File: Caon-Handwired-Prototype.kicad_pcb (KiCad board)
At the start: 6 copper layers, 28 parts, among them SW4 EC11 ENCODER 1, SW8 EC11 ENCODER 1, U1 74HC595, U2 74HC595, U3 SuperMini nRF52840

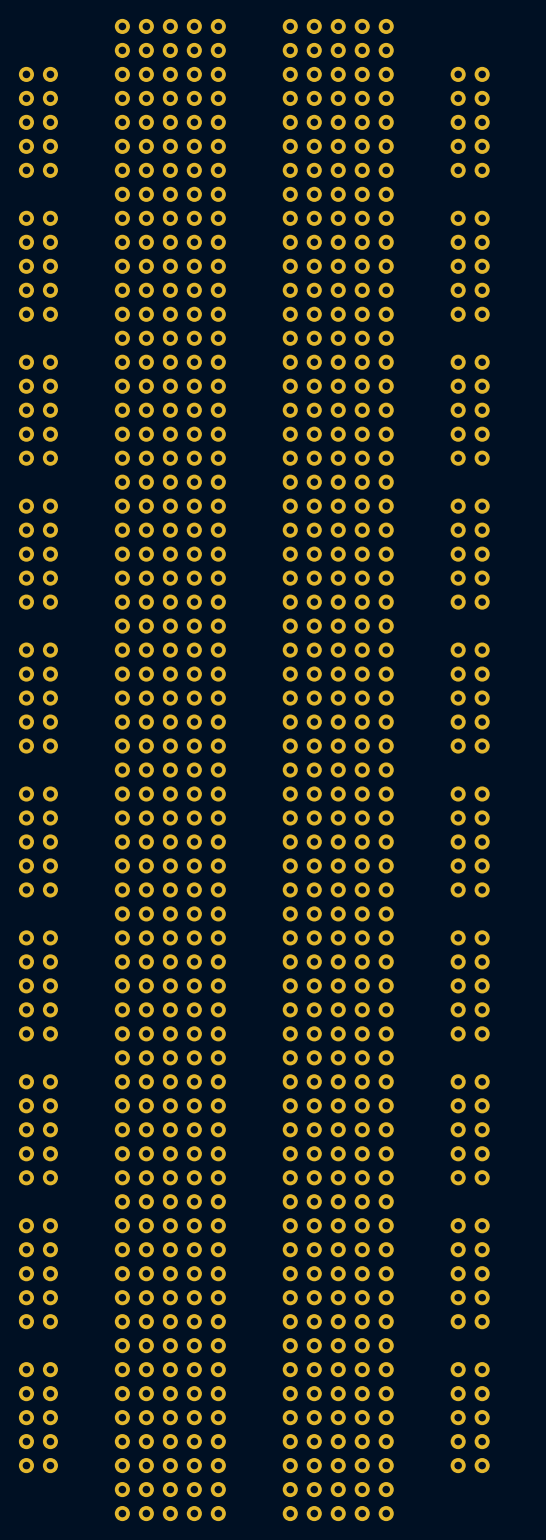
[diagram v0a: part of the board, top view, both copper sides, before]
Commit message: fix: 2nd 595 as 2nd Device
instead of daisy chained
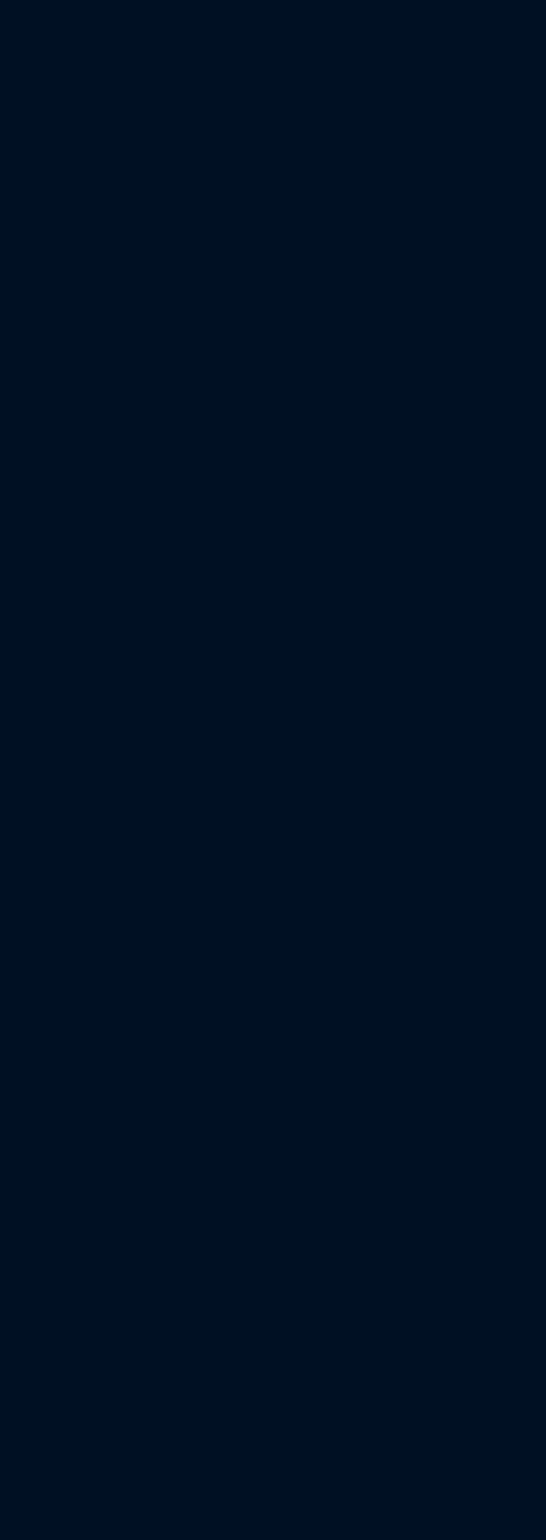
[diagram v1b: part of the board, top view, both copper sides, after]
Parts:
- removed REF**: Standard 830 Breadboard, Caon_Footprint:Standard 830 Breadboard
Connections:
- U1 pad 9: unconnected-(U1-QH&apos;-Pad9) -> QH'
- U2 pad 14: MOSI -> QH'
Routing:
- net MOSI: track 78.7 -> 48.3 mm
- net QH': track 0.00 -> 25.4 mm

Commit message: Schematic and PCB Update
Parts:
- added J1: OLED_128x32, ScottoKeebs_Components:OLED_128x32, F.Cu at (125.4, 37.9)
- added OLD_R1: 10k, Resistor_THT:R_Axial_DIN0204_L3.6mm_D1.6mm_P2.54mm_Vertical, F.Cu at (121.9, 37.6)
- added OLD_R2: 10k, Resistor_THT:R_Axial_DIN0204_L3.6mm_D1.6mm_P2.54mm_Vertical, F.Cu at (121.9, 45.2)
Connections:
- U3 pad 6: unconnected-(U3-P0.20-Pad6) -> SDA
- U3 pad 7: unconnected-(U3-P0.22-Pad7) -> SCL
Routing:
- net SDA: track 0.00 -> 27.9 mm
- net SCL: track 0.00 -> 27.9 mm
- net +3V3: track 342.9 -> 365.8 mm
- net GND: track 404.6 -> 414.8 mm

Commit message: Schematic Update
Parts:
- added REF**: MX_Solder_1.00u, ScottoKeebs_Scotto:MX_Solder_1.00u, F.Cu at (217.8, 71.7)
- added REF**: OLED_128x32, ScottoKeebs_Components:OLED_128x32, F.Cu at (236.1, 54.2)
- added REF**: MX_Solder_1.00u, ScottoKeebs_Scotto:MX_Solder_1.00u, F.Cu at (217.8, 52.7)
- added REF**: MX_Solder_1.00u, ScottoKeebs_Scotto:MX_Solder_1.00u, F.Cu at (217.8, 33.6)
- added REF**: MX_Solder_1.00u, ScottoKeebs_Scotto:MX_Solder_1.00u, F.Cu at (217.8, 109.8)
- added REF**: MX_Solder_1.00u, ScottoKeebs_Scotto:MX_Solder_1.00u, F.Cu at (236.9, 109.8)
- added REF**: MX_Solder_1.00u, ScottoKeebs_Scotto:MX_Solder_1.00u, F.Cu at (217.8, 90.8)
- added SW4: EC11 ENCODER 1, PCM_marbastlib-various:ROT_Alps_EC11E-Switch, F.Cu at (236.9, 90.8)
- added SW4: EC11 ENCODER 1, PCM_marbastlib-various:ROT_Alps_EC11E-Switch, F.Cu at (236.9, 71.7)
- added U3: SuperMini nRF52840, Caon_Footprint:SuperMini_NiceNano_USBdn, F.Cu at (236.9, 41.5)
